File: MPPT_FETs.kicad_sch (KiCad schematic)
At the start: 18 parts, among them U10 S130N10LF, U2 S130N10LF, U21 INA240A2D, U23 S130N10LF, U4 S130N10LF

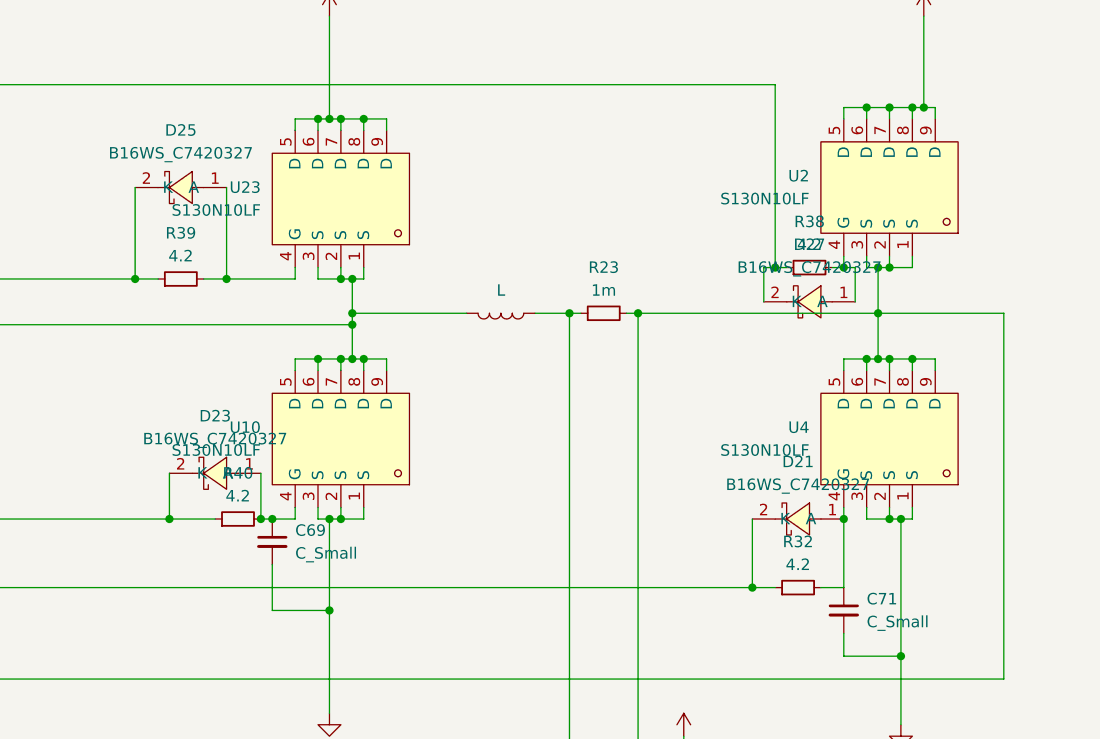
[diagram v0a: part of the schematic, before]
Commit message: latest version with PWM fan and thermistors for each FET bank
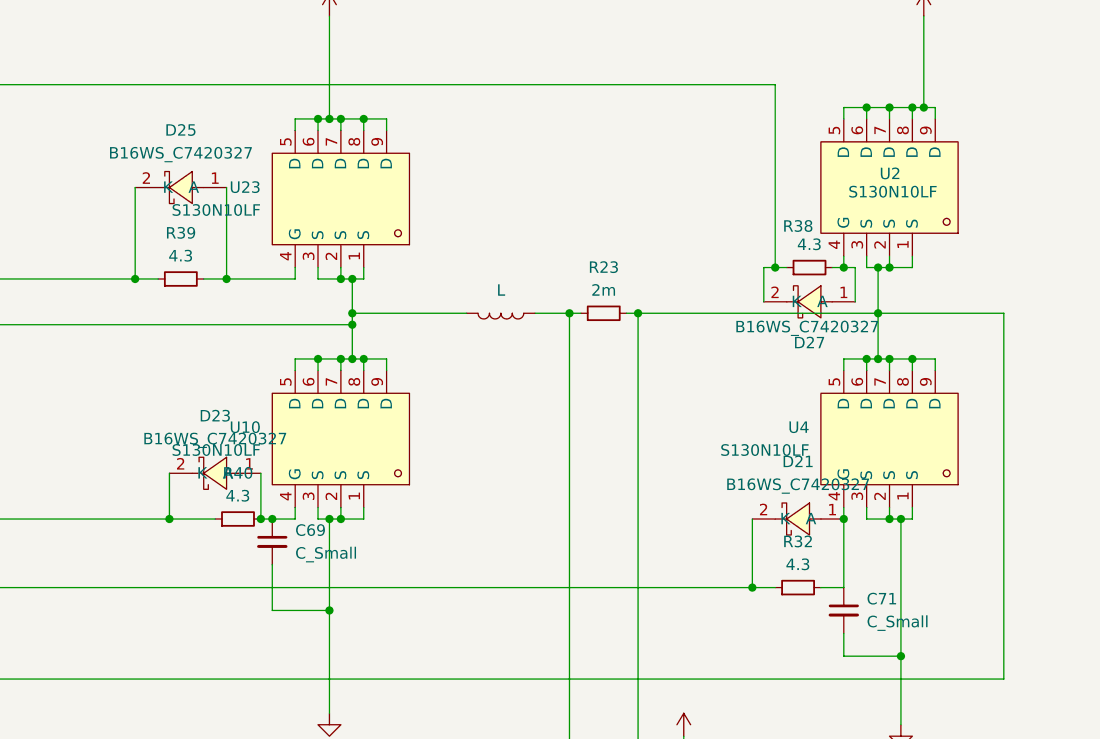
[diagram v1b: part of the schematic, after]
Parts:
- C61: LCSC Part (none) -> C880603
- C69, C71, L8: now left out of the parts list
- R23: value 1m -> 2m; LCSC Part (none) -> C160590
- R32, R38, R39, R40: value 4.2 -> 4.3; LCSC Part (none) -> C2930039
- U21: LCSC Part (none) -> C2060768
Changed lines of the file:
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@@
 		(unit 1)
 		(exclude_from_sim no)
-		(in_bom yes)
+		(in_bom no)
 		(on_board yes)
 		(dnp no)
@@
 			)
 		)
-		(property "Value" "4.2"
+		(property "Value" "4.3"
 			(at 170.18 105.41 90)
 			(effects
@@
 		(property "Description" "Resistor, small symbol"
 			(at 170.18 107.95 0)
+			(effects
+				(font
+					(size 1.27 1.27)
+				)
+				(hide yes)
+			)
+		)
+		(property "LCSC Part" "C2930039"
+			(at 170.18 107.95 90)
 			(effects
 				(font
@@
 			)
 		)
+		(property "LCSC Part" "C2060768"
+			(at 160.02 139.7 0)
+			(effects
+				(font
+					(size 1.27 1.27)
+				)
+				(hide yes)
+			)
+		)
 		(pin "6"
 		)
@@
 			)
 		)
-		(property "Value" "4.2"
+		(property "Value" "4.3"
 			(at 101.6 71.12 90)
 			(effects
@@
 		(property "Description" "Resistor, small symbol"
 			(at 101.6 73.66 0)
+			(effects
+				(font
+					(size 1.27 1.27)
+				)
+				(hide yes)
+			)
+		)
+		(property "LCSC Part" "C2930039"
+			(at 101.6 73.66 90)
 			(effects
 				(font
@@
 		(on_board yes)
 		(dnp no)
-		(fields_autoplaced yes)
 		(property "Reference" "R38"
-			(at 171.45 67.31 90)
-			(effects
-				(font
-					(size 1.27 1.27)
-				)
-			)
-		)
-		(property "Value" "4.2"
+			(at 170.18 67.818 90)
+			(effects
+				(font
+					(size 1.27 1.27)
+				)
+			)
+		)
+		(property "Value" "4.3"
 			(at 171.45 69.85 90)
 			(effects
@@
 		(property "Description" "Resistor, small symbol"
 			(at 171.45 72.39 0)
+			(effects
+				(font
+					(size 1.27 1.27)
+				)
+				(hide yes)
+			)
+		)
+		(property "LCSC Part" "C2930039"
+			(at 171.45 72.39 90)
 			(effects
 				(font
@@
 		(unit 1)
 		(exclude_from_sim no)
-		(in_bom yes)
+		(in_bom no)
 		(on_board yes)
 		(dnp no)
@@
 		(dnp no)
 		(property "Reference" "U2"
-			(at 171.45 62.2299 90)
+			(at 181.61 61.976 90)
 			(effects
 				(font
@@
 		)
 		(property "Value" "S130N10LF"
-			(at 171.45 64.7699 90)
+			(at 185.674 64.008 90)
 			(effects
 				(font
@@
 			)
 		)
-		(property "Value" "4.2"
+		(property "Value" "4.3"
 			(at 107.95 97.79 90)
 			(effects
@@
 			)
 		)
+		(property "LCSC Part" "C2930039"
+			(at 107.95 100.33 90)
+			(effects
+				(font
+					(size 1.27 1.27)
+				)
+				(hide yes)
+			)
+		)
 		(pin "2"
 		)
@@
 			)
 		)
+		(property "LCSC Part" "C880603"
+			(at 134.62 138.43 0)
+			(effects
+				(font
+					(size 1.27 1.27)
+				)
+				(hide yes)
+			)
+		)
 		(pin "1"
 		)
@@
 		(on_board yes)
 		(dnp no)
-		(fields_autoplaced yes)
 		(property "Reference" "D27"
-			(at 171.45 69.85 0)
+			(at 171.45 80.772 0)
 			(effects
 				(font
@@
 		)
 		(property "Value" "B16WS_C7420327"
-			(at 171.45 72.39 0)
+			(at 171.196 78.994 0)
 			(effects
 				(font
@@
 		(unit 1)
 		(exclude_from_sim no)
-		(in_bom yes)
+		(in_bom no)
 		(on_board yes)
 		(dnp no)
@@
 			)
 		)
-		(property "Value" "1m"
+		(property "Value" "2m"
 			(at 148.59 74.93 90)
 			(effects
@@
 			(effects
 				(font
+					(size 1.27 1.27)
+				)
+				(hide yes)
+			)
+		)
+		(property "LCSC Part" "C160590"
+			(at 148.59 77.47 90)
+			(effects
+				(font
